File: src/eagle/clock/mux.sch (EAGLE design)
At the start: 53 parts, among them U1 SN74HC595N, U2 SN74HC595N, U3 SN74HC595N

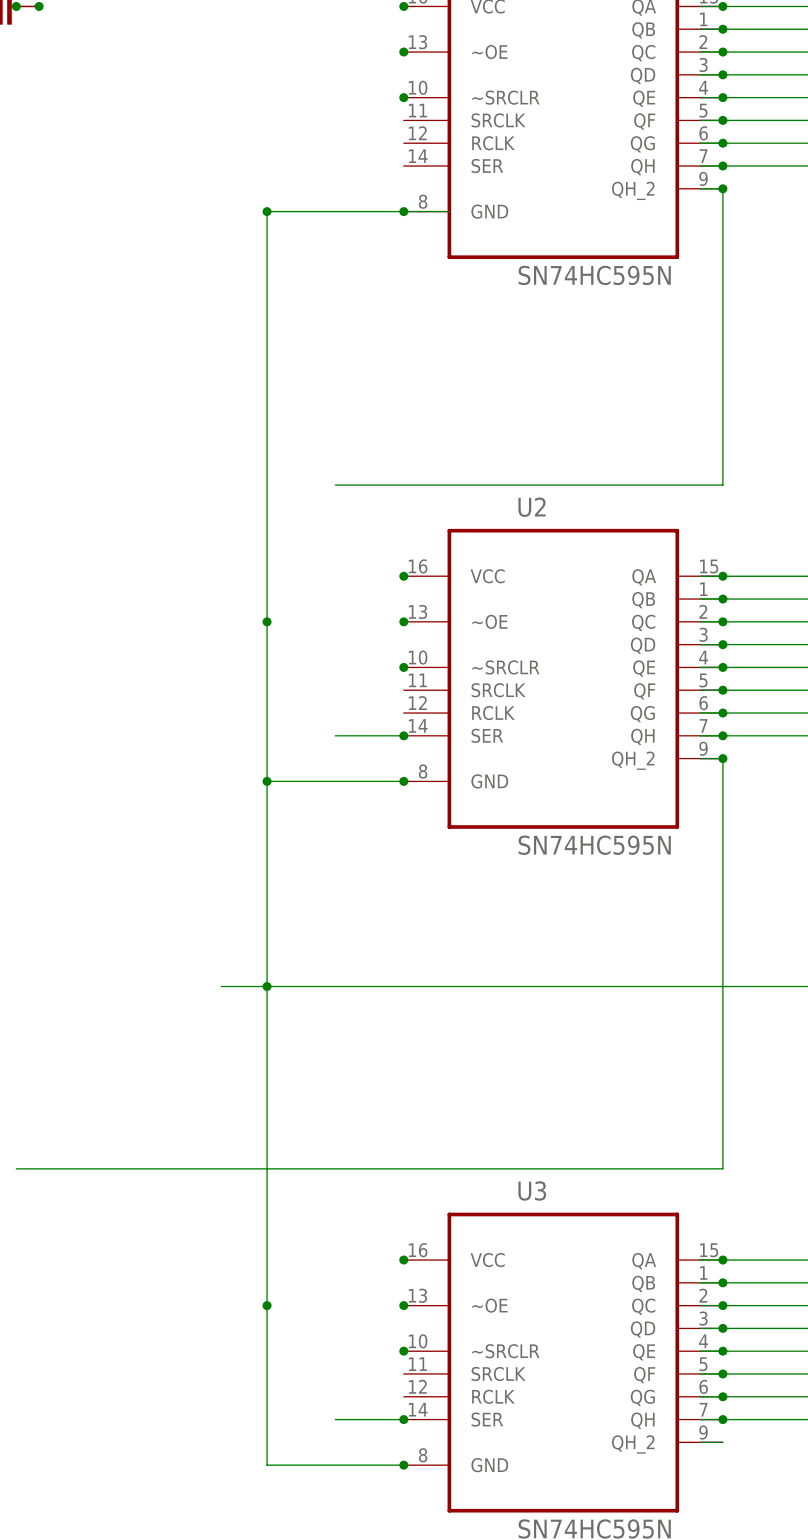
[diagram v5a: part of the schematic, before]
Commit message: AR12=>DSSRCLK(11)
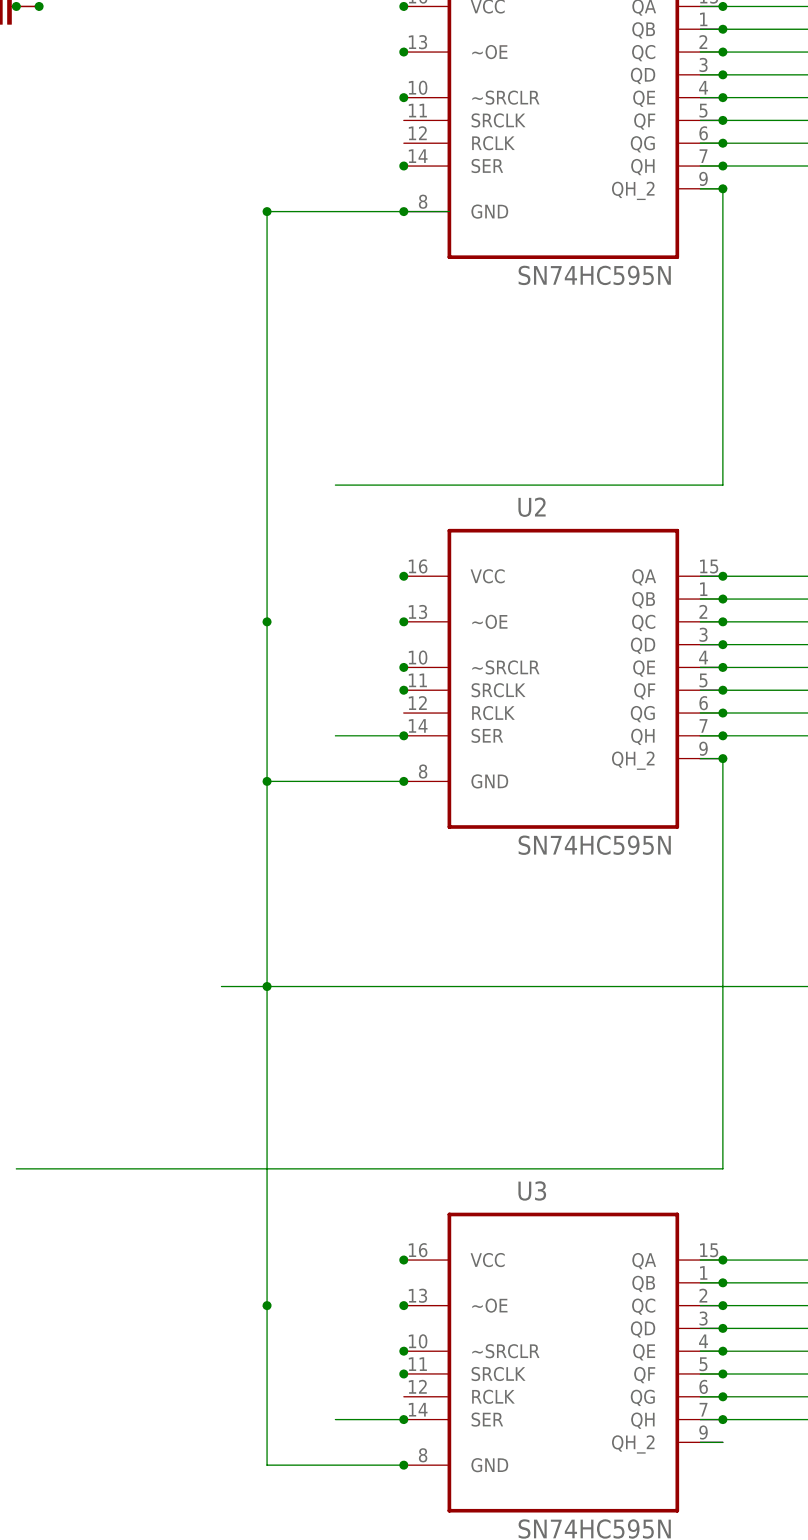
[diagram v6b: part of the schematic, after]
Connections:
- new net N$68: U3.SRCLK
- new net N$69: U2.RCLK
- new net N$70: U1.SER
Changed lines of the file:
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@@
 <plain>
 <wire x1="20.32" y1="60.96" x2="-7.62" y2="60.96" width="0.1524" layer="93"/>
-<wire x1="-7.62" y1="60.96" x2="-7.62" y2="50.8" width="0.1524" layer="93"/>
-<wire x1="-7.62" y1="50.8" x2="-7.62" y2="-2.54" width="0.1524" layer="93"/>
+<wire x1="-7.62" y1="60.96" x2="-7.62" y2="53.34" width="0.1524" layer="93"/>
+<wire x1="-7.62" y1="53.34" x2="-7.62" y2="10.16" width="0.1524" layer="93"/>
+<wire x1="-7.62" y1="5.08" x2="-7.62" y2="-2.54" width="0.1524" layer="93"/>
 <wire x1="-7.62" y1="-2.54" x2="2.54" y2="-2.54" width="0.1524" layer="93"/>
 <wire x1="7.62" y1="-2.54" x2="20.32" y2="-2.54" width="0.1524" layer="93"/>
@@
 <wire x1="20.32" y1="-7.62" x2="5.08" y2="-7.62" width="0.1524" layer="93"/>
 <wire x1="20.32" y1="-83.82" x2="5.08" y2="-83.82" width="0.1524" layer="93"/>
-<wire x1="20.32" y1="50.8" x2="-7.62" y2="50.8" width="0.1524" layer="93"/>
 <wire x1="20.32" y1="-12.7" x2="7.62" y2="-12.7" width="0.1524" layer="93"/>
 <wire x1="2.54" y1="-12.7" x2="-7.62" y2="-12.7" width="0.1524" layer="93"/>
@@
 <wire x1="2.54" y1="-96.52" x2="7.62" y2="-96.52" width="0.1524" layer="93" curve="-180"/>
 <wire x1="2.54" y1="-88.9" x2="7.62" y2="-88.9" width="0.1524" layer="93" curve="-180"/>
+<wire x1="-38.1" y1="22.86" x2="-25.4" y2="22.86" width="0.1524" layer="93"/>
+<wire x1="-25.4" y1="17.78" x2="-25.4" y2="-17.78" width="0.1524" layer="93"/>
+<wire x1="-25.4" y1="-17.78" x2="-25.4" y2="-45.72" width="0.1524" layer="93"/>
+<wire x1="-25.4" y1="-50.8" x2="-25.4" y2="-91.44" width="0.1524" layer="93"/>
+<wire x1="-20.32" y1="-91.44" x2="2.54" y2="-91.44" width="0.1524" layer="93"/>
+<wire x1="7.62" y1="-91.44" x2="20.32" y2="-91.44" width="0.1524" layer="93"/>
+<wire x1="2.54" y1="-91.44" x2="7.62" y2="-91.44" width="0.1524" layer="93" curve="-180"/>
+<wire x1="-25.4" y1="-91.44" x2="-20.32" y2="-91.44" width="0.1524" layer="93" curve="-180"/>
+<wire x1="-25.4" y1="-45.72" x2="-25.4" y2="-50.8" width="0.1524" layer="93" curve="-180"/>
+<wire x1="-25.4" y1="17.78" x2="-25.4" y2="22.86" width="0.1524" layer="93" curve="-180"/>
+<wire x1="-25.4" y1="-17.78" x2="-10.16" y2="-17.78" width="0.1524" layer="93"/>
+<wire x1="7.62" y1="-15.24" x2="20.32" y2="-15.24" width="0.1524" layer="93"/>
+<wire x1="-10.16" y1="-17.78" x2="-5.08" y2="-17.78" width="0.1524" layer="93" curve="-180"/>
+<wire x1="2.54" y1="-15.24" x2="7.62" y2="-15.24" width="0.1524" layer="93" curve="-180"/>
+<wire x1="0" y1="-17.78" x2="-5.08" y2="-17.78" width="0.1524" layer="93"/>
+<wire x1="-7.62" y1="10.16" x2="-7.62" y2="5.08" width="0.1524" layer="93" curve="-180"/>
+<wire x1="20.32" y1="48.26" x2="-5.08" y2="48.26" width="0.1524" layer="93"/>
+<wire x1="-10.16" y1="48.26" x2="-25.4" y2="48.26" width="0.1524" layer="93"/>
+<wire x1="-25.4" y1="48.26" x2="-25.4" y2="22.86" width="0.1524" layer="93"/>
+<wire x1="-10.16" y1="48.26" x2="-5.08" y2="48.26" width="0.1524" layer="93" curve="-180"/>
+<wire x1="-7.62" y1="53.34" x2="-2.54" y2="53.34" width="0.1524" layer="93"/>
+<wire x1="-2.54" y1="53.34" x2="-2.54" y2="50.8" width="0.1524" layer="93"/>
+<wire x1="-2.54" y1="50.8" x2="20.32" y2="50.8" width="0.1524" layer="93"/>
+<wire x1="2.54" y1="-15.24" x2="0" y2="-15.24" width="0.1524" layer="93"/>
+<wire x1="0" y1="-15.24" x2="0" y2="-17.78" width="0.1524" layer="93"/>
 </plain>
 <instances>
@@
 </segment>
 </net>
+<net name="N$68" class="0">
+<segment>
+<pinref part="U3" gate="A" pin="SRCLK"/>
+<junction x="20.32" y="-91.44"/>
+</segment>
+</net>
+<net name="N$69" class="0">
+<segment>
+<pinref part="U2" gate="A" pin="RCLK"/>
+<junction x="20.32" y="-15.24"/>
+</segment>
+</net>
+<net name="N$70" class="0">
+<segment>
+<pinref part="U1" gate="A" pin="SER"/>
+<junction x="20.32" y="43.18"/>
+</segment>
+</net>

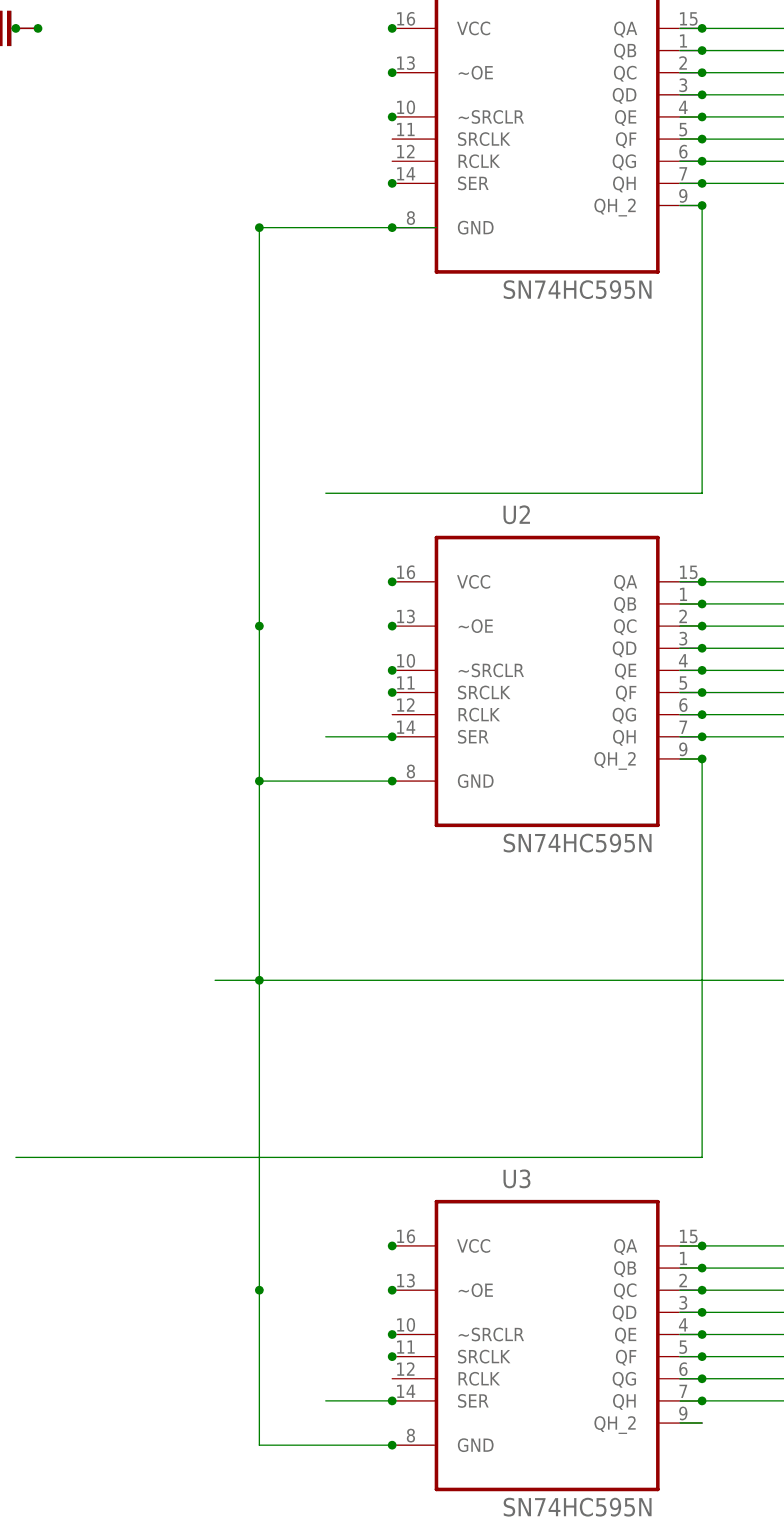
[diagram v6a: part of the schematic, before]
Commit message: ARD08=>SRRCLK(12)
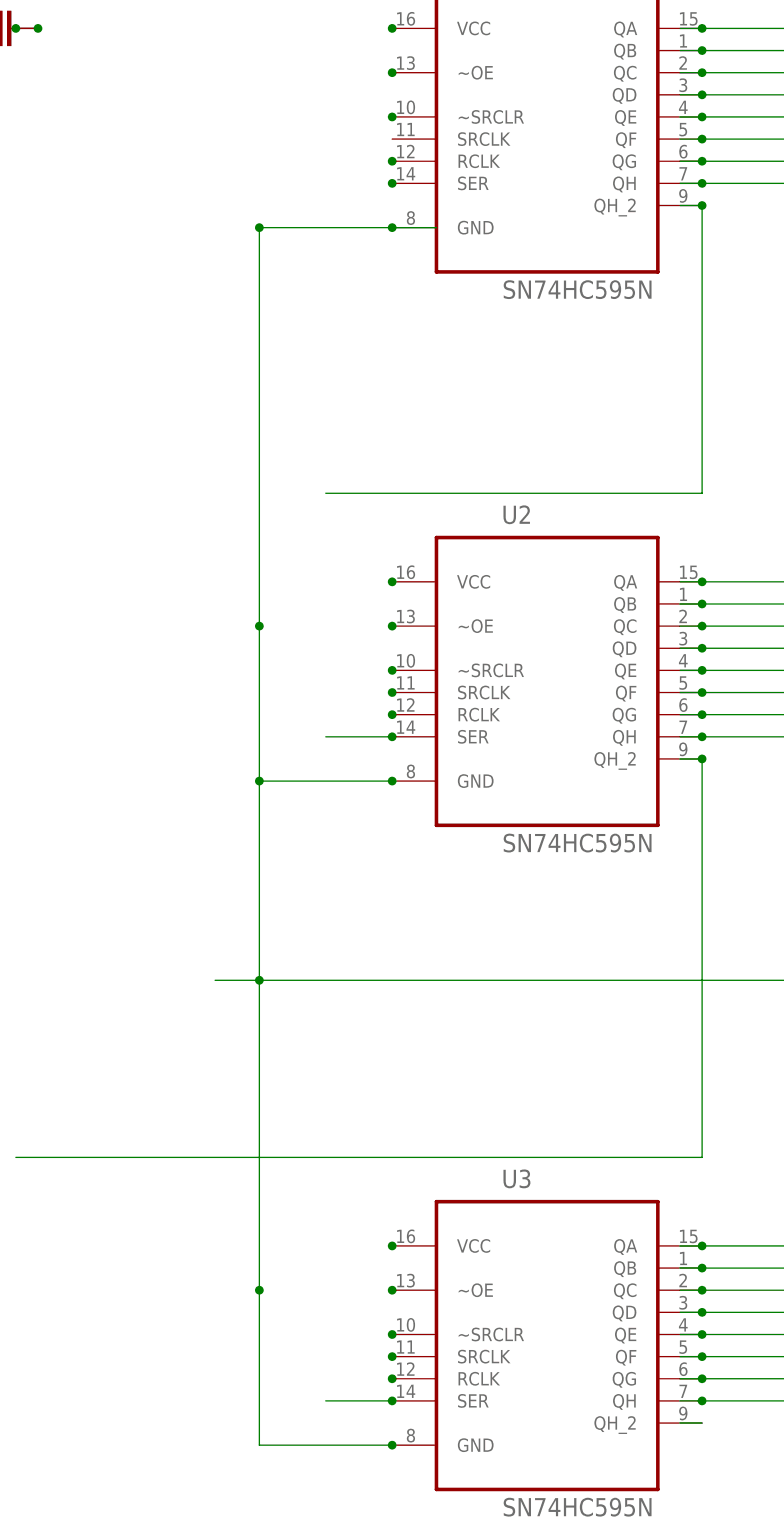
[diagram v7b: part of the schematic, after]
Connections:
- new net N$71: U3.RCLK
- new net N$72: U1.RCLK
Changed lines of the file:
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@@
 <wire x1="-116.84" y1="-48.26" x2="-116.84" y2="10.16" width="0.1524" layer="93"/>
 <wire x1="-116.84" y1="10.16" x2="-81.28" y2="10.16" width="0.1524" layer="93"/>
-<wire x1="-7.62" y1="-2.54" x2="-7.62" y2="-12.7" width="0.1524" layer="93"/>
-<wire x1="-7.62" y1="-12.7" x2="-7.62" y2="-78.74" width="0.1524" layer="93"/>
+<wire x1="-7.62" y1="-2.54" x2="-7.62" y2="-10.16" width="0.1524" layer="93"/>
+<wire x1="-7.62" y1="-10.16" x2="-7.62" y2="-78.74" width="0.1524" layer="93"/>
 <wire x1="-7.62" y1="-78.74" x2="-7.62" y2="-88.9" width="0.1524" layer="93"/>
 <wire x1="-116.84" y1="60.96" x2="-116.84" y2="15.24" width="0.1524" layer="93"/>
@@
 <wire x1="20.32" y1="-83.82" x2="5.08" y2="-83.82" width="0.1524" layer="93"/>
 <wire x1="20.32" y1="-12.7" x2="7.62" y2="-12.7" width="0.1524" layer="93"/>
-<wire x1="2.54" y1="-12.7" x2="-7.62" y2="-12.7" width="0.1524" layer="93"/>
+<wire x1="2.54" y1="-12.7" x2="-2.54" y2="-12.7" width="0.1524" layer="93"/>
 <wire x1="20.32" y1="-88.9" x2="7.62" y2="-88.9" width="0.1524" layer="93"/>
 <wire x1="2.54" y1="-88.9" x2="-7.62" y2="-88.9" width="0.1524" layer="93"/>
@@
 <wire x1="2.54" y1="-78.74" x2="7.62" y2="-78.74" width="0.1524" layer="93" curve="-180"/>
 <wire x1="12.7" y1="7.62" x2="-22.86" y2="7.62" width="0.1524" layer="93"/>
-<wire x1="-22.86" y1="7.62" x2="-22.86" y2="-20.32" width="0.1524" layer="93"/>
+<wire x1="-22.86" y1="7.62" x2="-22.86" y2="-7.62" width="0.1524" layer="93"/>
+<wire x1="-22.86" y1="-12.7" x2="-22.86" y2="-20.32" width="0.1524" layer="93"/>
 <wire x1="-22.86" y1="-20.32" x2="-10.16" y2="-20.32" width="0.1524" layer="93"/>
 <wire x1="-5.08" y1="-20.32" x2="2.54" y2="-20.32" width="0.1524" layer="93"/>
@@
 <wire x1="2.54" y1="-88.9" x2="7.62" y2="-88.9" width="0.1524" layer="93" curve="-180"/>
 <wire x1="-38.1" y1="22.86" x2="-25.4" y2="22.86" width="0.1524" layer="93"/>
-<wire x1="-25.4" y1="17.78" x2="-25.4" y2="-17.78" width="0.1524" layer="93"/>
-<wire x1="-25.4" y1="-17.78" x2="-25.4" y2="-45.72" width="0.1524" layer="93"/>
-<wire x1="-25.4" y1="-50.8" x2="-25.4" y2="-91.44" width="0.1524" layer="93"/>
-<wire x1="-20.32" y1="-91.44" x2="2.54" y2="-91.44" width="0.1524" layer="93"/>
+<wire x1="-25.4" y1="17.78" x2="-25.4" y2="-10.16" width="0.1524" layer="93"/>
+<wire x1="-25.4" y1="-10.16" x2="-25.4" y2="-45.72" width="0.1524" layer="93"/>
+<wire x1="-25.4" y1="-50.8" x2="-25.4" y2="-86.36" width="0.1524" layer="93"/>
+<wire x1="-15.24" y1="-91.44" x2="2.54" y2="-91.44" width="0.1524" layer="93"/>
 <wire x1="7.62" y1="-91.44" x2="20.32" y2="-91.44" width="0.1524" layer="93"/>
 <wire x1="2.54" y1="-91.44" x2="7.62" y2="-91.44" width="0.1524" layer="93" curve="-180"/>
-<wire x1="-25.4" y1="-91.44" x2="-20.32" y2="-91.44" width="0.1524" layer="93" curve="-180"/>
 <wire x1="-25.4" y1="-45.72" x2="-25.4" y2="-50.8" width="0.1524" layer="93" curve="-180"/>
 <wire x1="-25.4" y1="17.78" x2="-25.4" y2="22.86" width="0.1524" layer="93" curve="-180"/>
-<wire x1="-25.4" y1="-17.78" x2="-10.16" y2="-17.78" width="0.1524" layer="93"/>
 <wire x1="7.62" y1="-15.24" x2="20.32" y2="-15.24" width="0.1524" layer="93"/>
-<wire x1="-10.16" y1="-17.78" x2="-5.08" y2="-17.78" width="0.1524" layer="93" curve="-180"/>
+<wire x1="-10.16" y1="-15.24" x2="-5.08" y2="-15.24" width="0.1524" layer="93" curve="-180"/>
 <wire x1="2.54" y1="-15.24" x2="7.62" y2="-15.24" width="0.1524" layer="93" curve="-180"/>
-<wire x1="0" y1="-17.78" x2="-5.08" y2="-17.78" width="0.1524" layer="93"/>
+<wire x1="2.54" y1="-15.24" x2="-5.08" y2="-15.24" width="0.1524" layer="93"/>
 <wire x1="-7.62" y1="10.16" x2="-7.62" y2="5.08" width="0.1524" layer="93" curve="-180"/>
 <wire x1="20.32" y1="48.26" x2="-5.08" y2="48.26" width="0.1524" layer="93"/>
@@
 <wire x1="-2.54" y1="53.34" x2="-2.54" y2="50.8" width="0.1524" layer="93"/>
 <wire x1="-2.54" y1="50.8" x2="20.32" y2="50.8" width="0.1524" layer="93"/>
-<wire x1="2.54" y1="-15.24" x2="0" y2="-15.24" width="0.1524" layer="93"/>
-<wire x1="0" y1="-15.24" x2="0" y2="-17.78" width="0.1524" layer="93"/>
+<wire x1="-7.62" y1="-10.16" x2="-2.54" y2="-10.16" width="0.1524" layer="93"/>
+<wire x1="-2.54" y1="-10.16" x2="-2.54" y2="-12.7" width="0.1524" layer="93"/>
+<wire x1="-25.4" y1="-10.16" x2="-15.24" y2="-10.16" width="0.1524" layer="93"/>
+<wire x1="-15.24" y1="-10.16" x2="-15.24" y2="-15.24" width="0.1524" layer="93"/>
+<wire x1="-15.24" y1="-15.24" x2="-10.16" y2="-15.24" width="0.1524" layer="93"/>
+<wire x1="-20.32" y1="-86.36" x2="-15.24" y2="-86.36" width="0.1524" layer="93"/>
+<wire x1="-15.24" y1="-86.36" x2="-15.24" y2="-91.44" width="0.1524" layer="93"/>
+<wire x1="-25.4" y1="-86.36" x2="-20.32" y2="-86.36" width="0.1524" layer="93" curve="-180"/>
+<wire x1="-22.86" y1="-7.62" x2="-22.86" y2="-12.7" width="0.1524" layer="93" curve="-180"/>
+<wire x1="-38.1" y1="12.7" x2="-33.02" y2="12.7" width="0.1524" layer="93"/>
+<wire x1="-33.02" y1="12.7" x2="-33.02" y2="-17.78" width="0.1524" layer="93"/>
+<wire x1="-20.32" y1="-17.78" x2="-10.16" y2="-17.78" width="0.1524" layer="93"/>
+<wire x1="-5.08" y1="-17.78" x2="2.54" y2="-17.78" width="0.1524" layer="93"/>
+<wire x1="7.62" y1="-17.78" x2="20.32" y2="-17.78" width="0.1524" layer="93"/>
+<wire x1="-27.94" y1="-17.78" x2="-20.32" y2="-17.78" width="0.1524" layer="93" curve="-180"/>
+<wire x1="-10.16" y1="-17.78" x2="-5.08" y2="-17.78" width="0.1524" layer="93" curve="-180"/>
+<wire x1="2.54" y1="-17.78" x2="7.62" y2="-17.78" width="0.1524" layer="93" curve="-180"/>
+<wire x1="-33.02" y1="12.7" x2="-27.94" y2="12.7" width="0.1524" layer="93"/>
+<wire x1="-22.86" y1="12.7" x2="-10.16" y2="12.7" width="0.1524" layer="93"/>
+<wire x1="-5.08" y1="12.7" x2="2.54" y2="12.7" width="0.1524" layer="93"/>
+<wire x1="7.62" y1="12.7" x2="10.16" y2="12.7" width="0.1524" layer="93"/>
+<wire x1="10.16" y1="12.7" x2="10.16" y2="35.56" width="0.1524" layer="93"/>
+<wire x1="10.16" y1="45.72" x2="20.32" y2="45.72" width="0.1524" layer="93"/>
+<wire x1="-27.94" y1="12.7" x2="-22.86" y2="12.7" width="0.1524" layer="93" curve="-180"/>
+<wire x1="-10.16" y1="12.7" x2="-5.08" y2="12.7" width="0.1524" layer="93" curve="-180"/>
+<wire x1="2.54" y1="12.7" x2="7.62" y2="12.7" width="0.1524" layer="93" curve="-180"/>
+<wire x1="10.16" y1="45.72" x2="10.16" y2="40.64" width="0.1524" layer="93" curve="-180"/>
+<wire x1="10.16" y1="40.64" x2="10.16" y2="35.56" width="0.1524" layer="93" curve="-180"/>
+<wire x1="-33.02" y1="-17.78" x2="-27.94" y2="-17.78" width="0.1524" layer="93"/>
+<wire x1="-27.94" y1="-17.78" x2="-27.94" y2="-45.72" width="0.1524" layer="93"/>
+<wire x1="-27.94" y1="-50.8" x2="-27.94" y2="-93.98" width="0.1524" layer="93"/>
+<wire x1="-27.94" y1="-93.98" x2="-25.4" y2="-93.98" width="0.1524" layer="93"/>
+<wire x1="-20.32" y1="-93.98" x2="2.54" y2="-93.98" width="0.1524" layer="93"/>
+<wire x1="7.62" y1="-93.98" x2="20.32" y2="-93.98" width="0.1524" layer="93"/>
+<wire x1="-25.4" y1="-93.98" x2="-20.32" y2="-93.98" width="0.1524" layer="93" curve="-180"/>
+<wire x1="2.54" y1="-93.98" x2="7.62" y2="-93.98" width="0.1524" layer="93" curve="-180"/>
+<wire x1="-27.94" y1="-45.72" x2="-27.94" y2="-50.8" width="0.1524" layer="93" curve="-180"/>
 </plain>
 <instances>
@@
 <pinref part="U2" gate="A" pin="RCLK"/>
 <junction x="20.32" y="-15.24"/>
+<junction x="20.32" y="-17.78"/>
 </segment>
 </net>
@@
 </segment>
 </net>
+<net name="N$71" class="0">
+<segment>
+<pinref part="U3" gate="A" pin="RCLK"/>
+<junction x="20.32" y="-93.98"/>
+</segment>
+</net>
+<net name="N$72" class="0">
+<segment>
+<pinref part="U1" gate="A" pin="RCLK"/>
+<junction x="20.32" y="45.72"/>
+</segment>
+</net>
